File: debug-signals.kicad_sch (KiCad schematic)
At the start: 77 parts, among them U10 TCA9534PWR, U11 TCA9534PWR, U12 Si7021, U13 TCA9534PWR, U14 TCA9534PWR

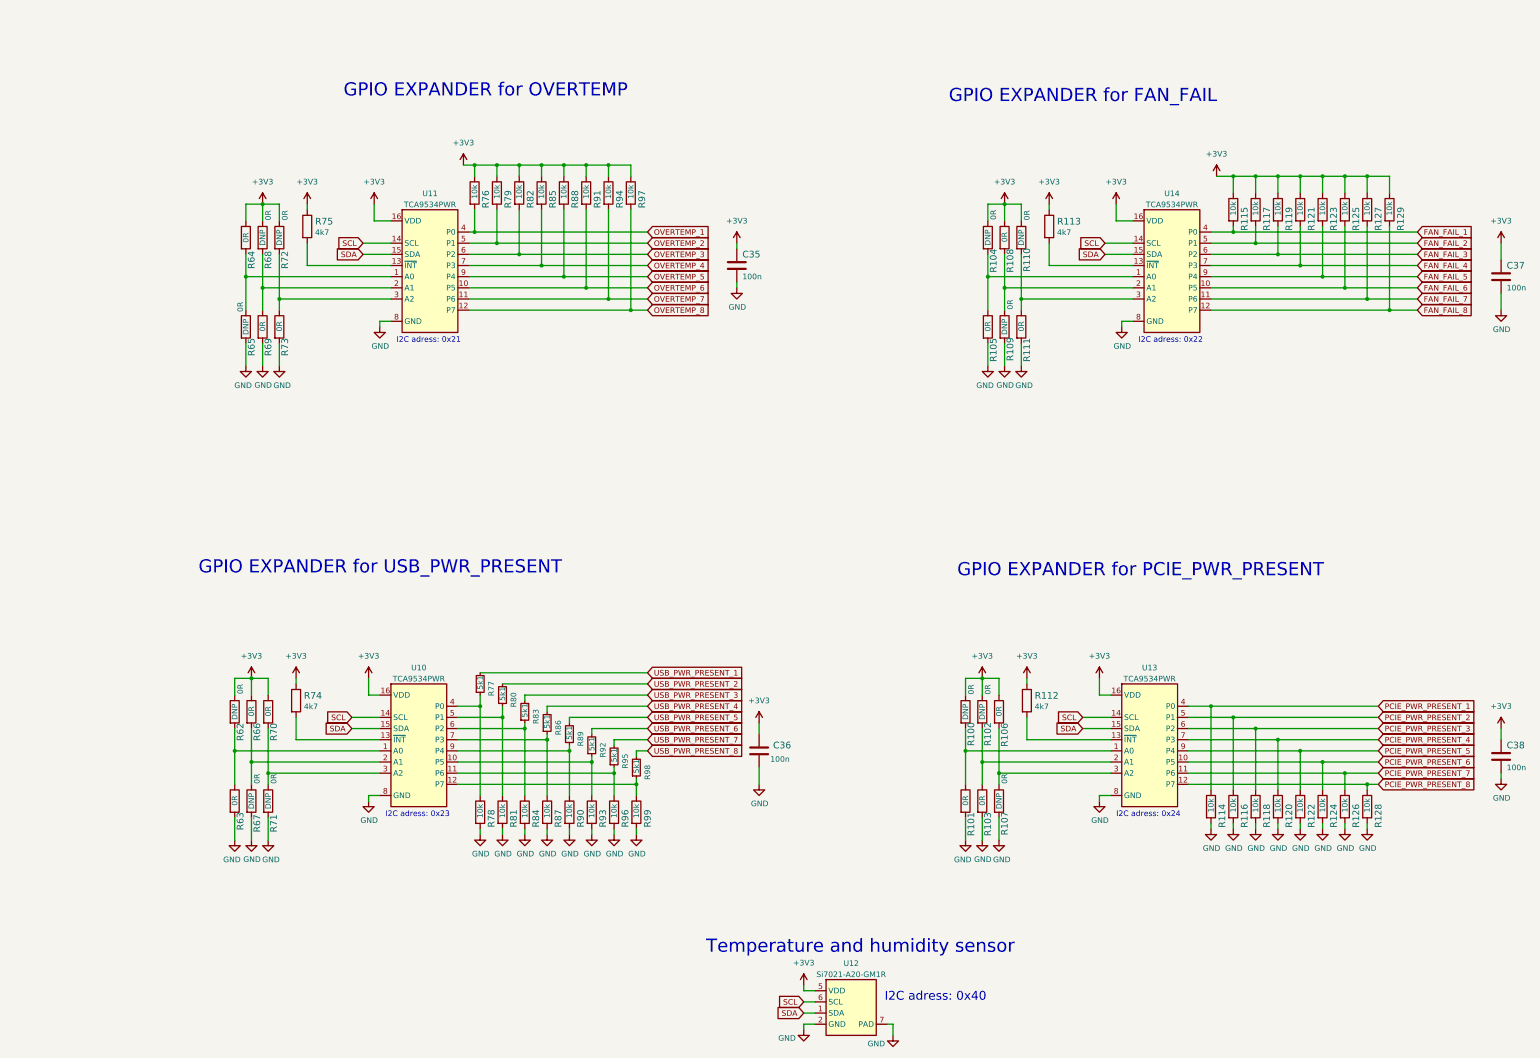
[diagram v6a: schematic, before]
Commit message: Standarize debug signal schematic
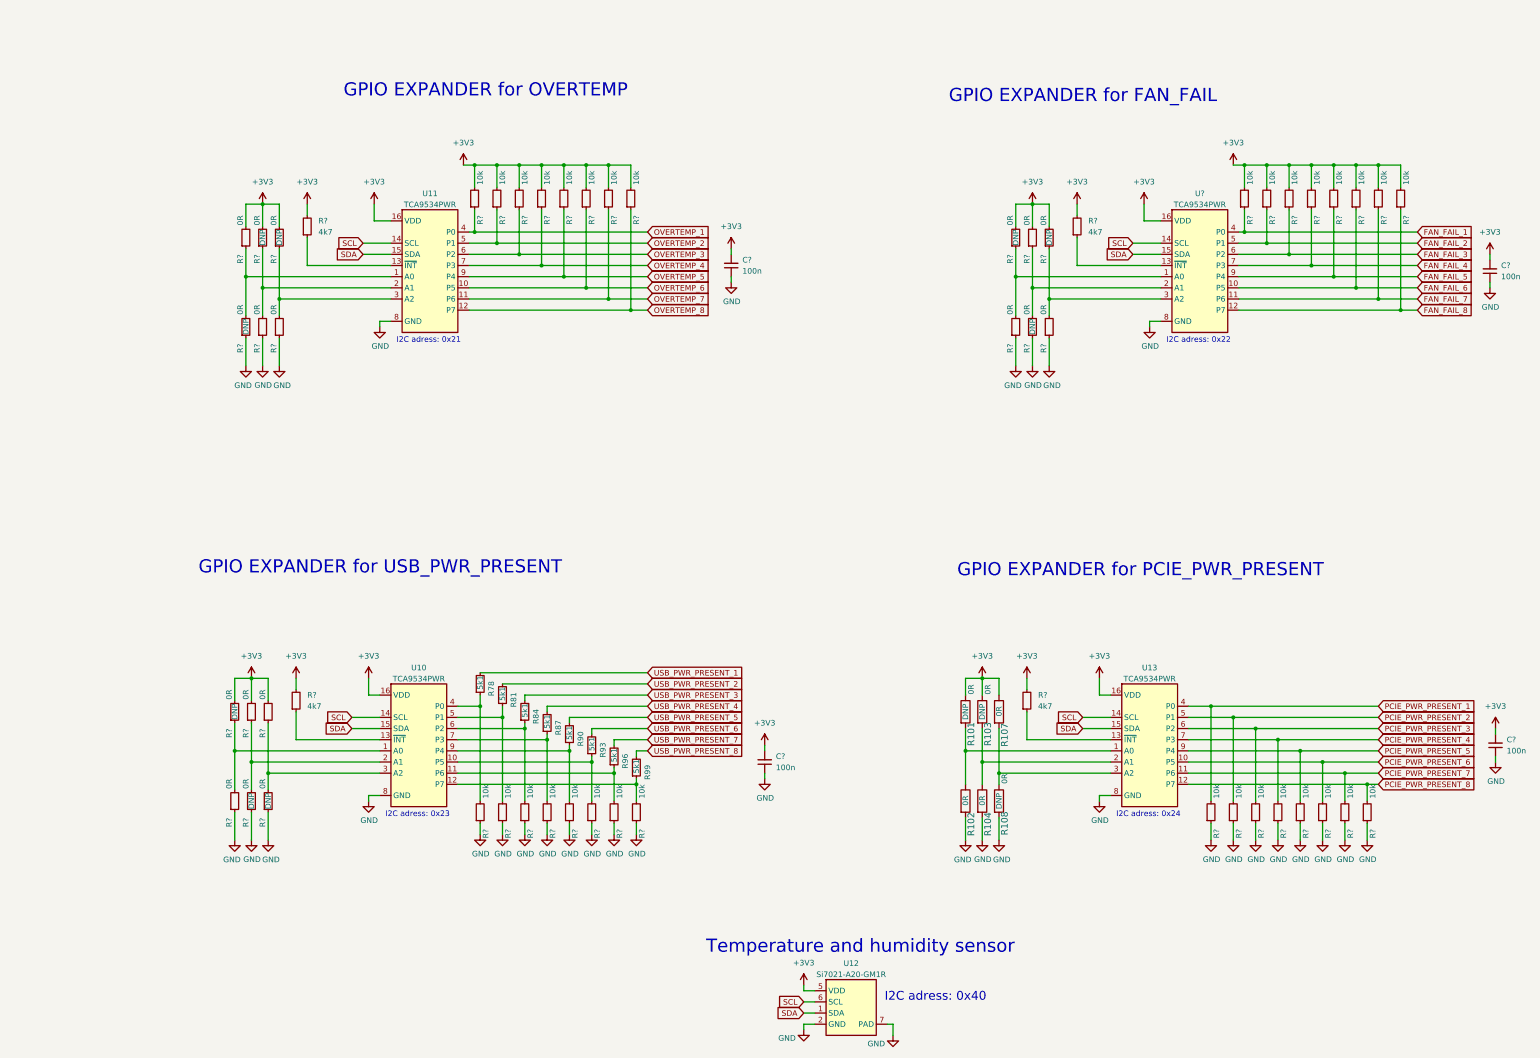
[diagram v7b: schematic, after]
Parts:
- removed C35, C36, C37, C38: C_100n_0402, antmicro-footprints:C_0402_1005Metric, symbol antmicroCapacitors0402:C_100n_0402
- removed R104, R105, R108, R109, R110, R111, R62, R63, R64, R65, R66, R67, R68, R69, R70, R71, R72, R73: R_0R_0402, antmicro-footprints:R_0402_1005Metric, symbol antmicroResistors0402:R_0R_0402
- removed R112, R113, R74, R75: R_4k7_0402, antmicro-footprints:R_0402_1005Metric, symbol antmicroResistors0402:R_4k7_0402
- removed R114, R115, R116, R117, R118, R119, R120, R121, R122, R123, R124, R125, R126, R127, R128, R129, R76, R78, R79, R81, R82, R84, R85, R87, R88, R90, R91, R93, R94, R96, R97, R99: R_10k_0402, antmicro-footprints:R_0402_1005Metric, symbol antmicroResistors0402:R_10k_0402
- removed U14: TCA9534PWR, antmicro-footprints:TSSOP-16_4.4x5mm_P0.65mm, symbol antmicroInterfaceIOExpanders:TCA9534PWR
- added C? (x4): C_100n_0402, antmicro-footprints:C_0402_1005Metric, symbol antmicroCapacitors0402:C_100n_0402
- added R? (x32): R_10k_0402, antmicro-footprints:R_0402_1005Metric, symbol antmicroResistors0402:R_10k_0402
- added R? (x18): R_0R_0402, antmicro-footprints:R_0402_1005Metric, symbol antmicroResistors0402:R_0R_0402
- added R? (x4): R_4k7_0402, antmicro-footprints:R_0402_1005Metric, symbol antmicroResistors0402:R_4k7_0402
- added U?: TCA9534PWR, antmicro-footprints:TSSOP-16_4.4x5mm_P0.65mm, symbol antmicroInterfaceIOExpanders:TCA9534PWR
- renumbered R100 to R101, R101 to R102, R102 to R103, R103 to R104, R106 to R107, R107 to R108, R77 to R78, R80 to R81, R83 to R84, R86 to R87, R89 to R90, R92 to R93, R95 to R96, R98 to R99
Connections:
- net +3V3: now also C?.2, C?.2, C?.2, C?.2, R?.2, R?.2, R?.2, R?.2, R?.2, R?.2, R?.2, R?.2, R?.2, R?.2, R?.2, R?.2, R?.2, R?.2, R?.2, R?.2, R?.2, R?.2, R?.2, R?.2, R?.2, R?.2, R?.2, R?.2, R?.2, R?.2, R?.2, R?.2, R?.2, U?.16 (VDD)
- net FAN_FAIL_1: now also R?.1, U?.4 (P0)
- net FAN_FAIL_2: now also R?.1, U?.5 (P1)
- net FAN_FAIL_3: now also R?.1, U?.6 (P2)
- net FAN_FAIL_4: now also R?.1, U?.7 (P3)
- net FAN_FAIL_5: now also R?.1, U?.9 (P4)
- net FAN_FAIL_6: now also R?.1, U?.10 (P5)
- net FAN_FAIL_7: now also R?.1, U?.11 (P6)
- net FAN_FAIL_8: now also R?.1, U?.12 (P7)
- net GND: now also C?.1, C?.1, C?.1, C?.1, R?.1, R?.1, R?.1, R?.1, R?.1, R?.1, R?.1, R?.1, R?.1, R?.1, R?.1, R?.1, R?.1, R?.1, R?.1, R?.1, R?.1, R?.1, R?.1, R?.1, R?.1, R?.1, R?.1, R?.1, R?.1, U?.8 (GND)
- net OVERTEMP_1: now also R?.1
- net OVERTEMP_2: now also R?.1
- net OVERTEMP_3: now also R?.1
- net OVERTEMP_4: now also R?.1
- net OVERTEMP_5: now also R?.1
- net OVERTEMP_6: now also R?.1
- net OVERTEMP_7: now also R?.1
- net OVERTEMP_8: now also R?.1
- net PCIE_PWR_PRESENT_1: now also R?.2
- net PCIE_PWR_PRESENT_2: now also R?.2
- net PCIE_PWR_PRESENT_3: now also R?.2
- net PCIE_PWR_PRESENT_4: now also R?.2
- net PCIE_PWR_PRESENT_5: now also R?.2
- net PCIE_PWR_PRESENT_6: now also R?.2
- net PCIE_PWR_PRESENT_7: now also R?.2
- net PCIE_PWR_PRESENT_8: now also R?.2
- net SCL: now also U?.14 (SCL)
- net SDA: now also U?.15 (SDA)
- net at R96.1, U10.11 (P6): now also R?.2
- net at R90.1, U10.9 (P4): now also R?.2
- net at U10.1 (A0): now also R?.1, R?.2
- net at R93.1, U10.10 (P5): now also R?.2
- net at R99.1, U10.12 (P7): now also R?.2
- net at U10.13 (~{INT}): now also R?.1
- net at U10.2 (A1): now also R?.1, R?.2
- net at U10.3 (A2): now also R?.1, R?.2
- net at R78.1, U10.4 (P0): now also R?.2
- net at R81.1, U10.5 (P1): now also R?.2
- net at R84.1, U10.6 (P2): now also R?.2
- net at R87.1, U10.7 (P3): now also R?.2
- net at U11.1 (A0): now also R?.1, R?.2
- net at U11.13 (~{INT}): now also R?.1
- net at U11.2 (A1): now also R?.1, R?.2
- net at U11.3 (A2): now also R?.1, R?.2
- net at U13.13 (~{INT}): now also R?.1
- new net: R?.1, R?.2, U?.1 (A0)
- new net: R?.1, U?.13 (~{INT})
- new net: R?.1, R?.2, U?.2 (A1)
- new net: R?.1, R?.2, U?.3 (A2)

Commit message: Standarize fans control
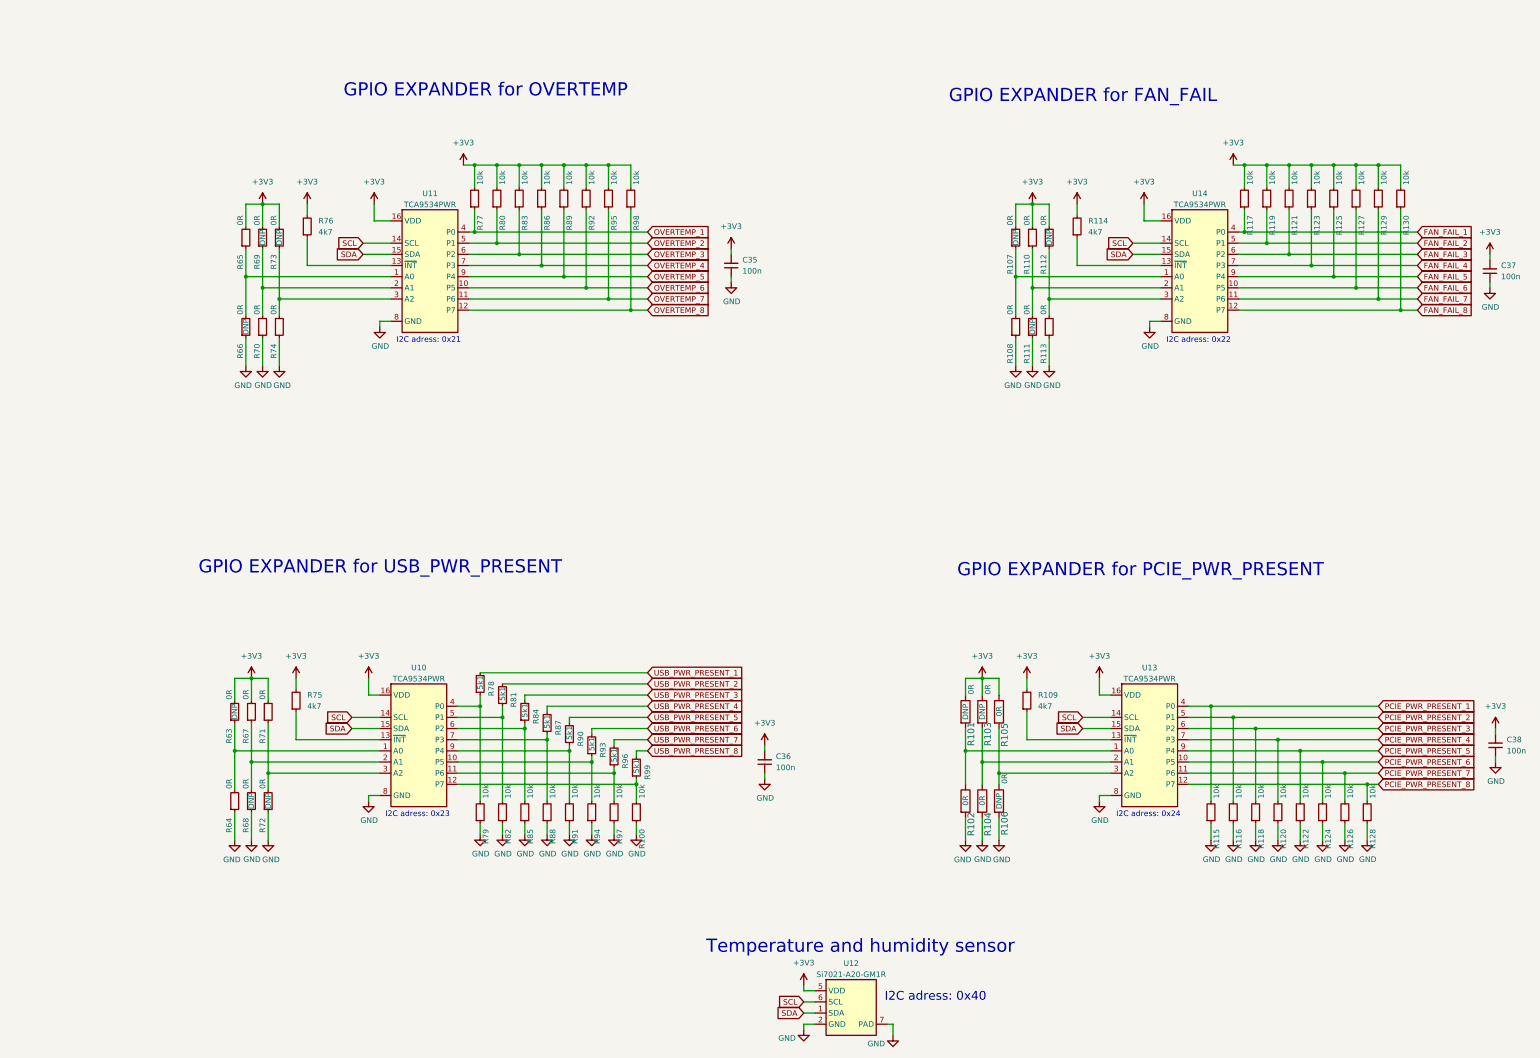
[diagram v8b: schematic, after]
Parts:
- gave numbers to parts that had none: 59
- renumbered R107 to R105, R108 to R106
